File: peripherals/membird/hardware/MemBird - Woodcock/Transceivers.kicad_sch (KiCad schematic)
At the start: 23 parts, among them U10 74HC86, U11 74LS20, U13 74LS32, U14 74LS32, U4 74HC14, U5 74LVC16245DG, U6 74LS139, U8 74LVCC3245APWR, U9 74LVC16245DG

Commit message: MemBird - Woodcock Rev.1 Schematic is complete
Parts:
- removed C11, C12, C13, C14, C15, C16: 0.1uF, Capacitor_SMD:C_0805_2012Metric_Pad1.18x1.45mm_HandSolder, symbol Device:C_Small
- removed JP1: A22, symbol Jumper:Jumper_3_Bridged12
- removed JP2: A23, symbol Jumper:Jumper_3_Bridged12
- removed U10: 74HC86, symbol 74xx:74HC86
- removed U11: 74LS20, symbol 74xx:74LS20
- removed U13, U14: 74LS32, symbol 74xx:74LS32
- removed unit 4 of U4
- removed unit 7 of U4
- removed unit 2 of U4
- removed unit 3 of U4
- removed U6: 74LS139, symbol 74xx:74LS139
- U13: renamed from U5; value 74LVC16245DG -> 74ALVC164245DG
- U15: renamed from U9; value 74LVC16245DG -> 74ALVC164245DG
- U3: renamed from U4; footprint (none) -> Package_SO:TSSOP-14_4.4x5mm_P0.65mm
- renumbered C3 to C12, C7 to C13, C4 to C14, C8 to C15, C9 to C16, C10 to C17, U8 to U14
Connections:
- net +3.3V is gone; now on net VMEM: C14.1, C15.1, C17.1, U13.31 (VCCa), U13.42 (VCCa), U14.1 (VCCa), U15.31 (VCCa), U15.42 (VCCa)
- net ~{RD}: now also U3.8; no longer U3.2
- net ~{WR}: now also U3.9; no longer U3.1
- no-connect marks 1 -> 8
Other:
- note removed: "TODO: do you need a timer here"
- note removed: "TODO: handle berr signal"
- moved on the sheet: C12, C13, C14, C15, C16, C17, U13, U14, U15, U3D

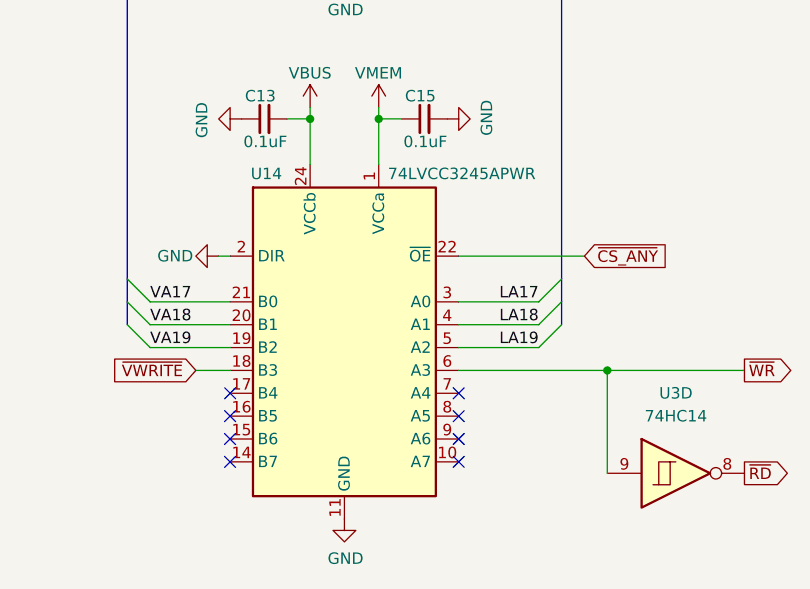
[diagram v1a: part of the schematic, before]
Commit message: Finished the MemBird - Woodcock 16-bit memory board layout
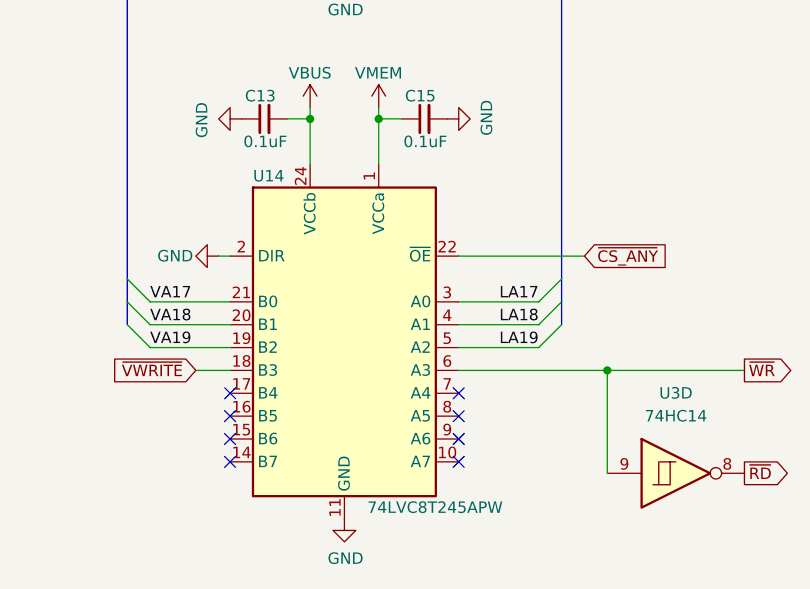
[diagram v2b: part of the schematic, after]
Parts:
- U14: value 74LVCC3245APWR -> 74LVC8T245APW; symbol Computie_Transceivers:74LVCC3245APWR -> Computie_Transceivers:74LVC8T245PW
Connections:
- net VBUS: now also U14.23 (VCCb)
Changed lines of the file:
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@@
 	)
 	(symbol
-		(lib_id "Computie_Transceivers:74LVCC3245APWR")
+		(lib_id "Computie_Transceivers:74LVC8T245PW")
 		(at 62.23 143.51 0)
 		(unit 1)
@@
 		(dnp no)
 		(property "Reference" "U14"
-			(at 51.816 125.476 0)
+			(at 52.07 125.73 0)
 			(effects
 				(font
@@
 			)
 		)
-		(property "Value" "74LVCC3245APWR"
-			(at 67.056 125.476 0)
+		(property "Value" "74LVC8T245APW"
+			(at 64.77 162.56 0)
 			(effects
 				(font
@@
 			)
 		)
-		(property "Datasheet" "https://assets.nexperia.com/documents/data-sheet/74ALVC164245.pdf"
+		(property "Datasheet" "https://assets.nexperia.com/documents/data-sheet/74LVC_LVCH8T245.pdf"
 			(at 62.23 158.75 0)
 			(effects
@@
 			)
 		)
-		(property "Description" ""
+		(property "Description" "8-Bit Dual Supply Bidirectional Translating Transceiver with 5V Tolerant Inputs and Outputs, TSSOP-24"
 			(at 62.23 143.51 0)
 			(effects
